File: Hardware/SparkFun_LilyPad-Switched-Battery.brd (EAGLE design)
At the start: 29.4 x 29.2 mm, 11 parts

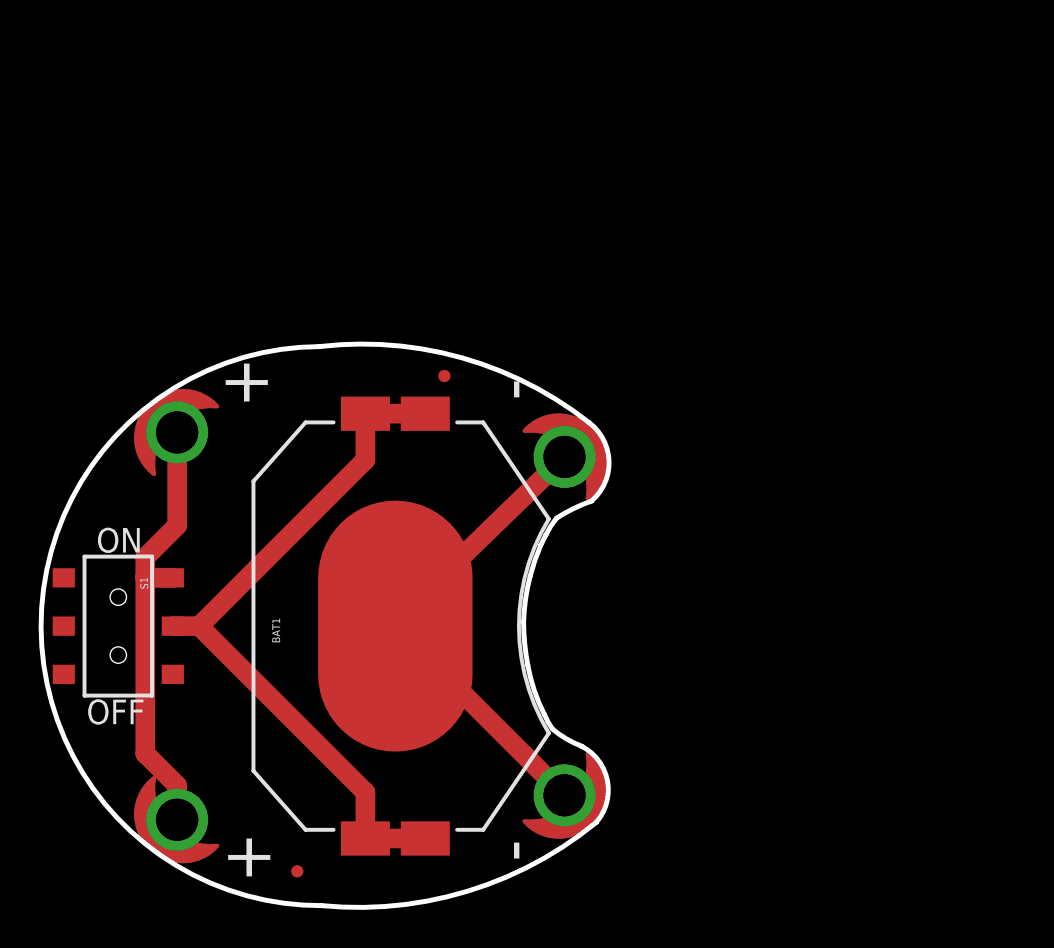
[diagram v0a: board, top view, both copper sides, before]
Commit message: Add board thickness
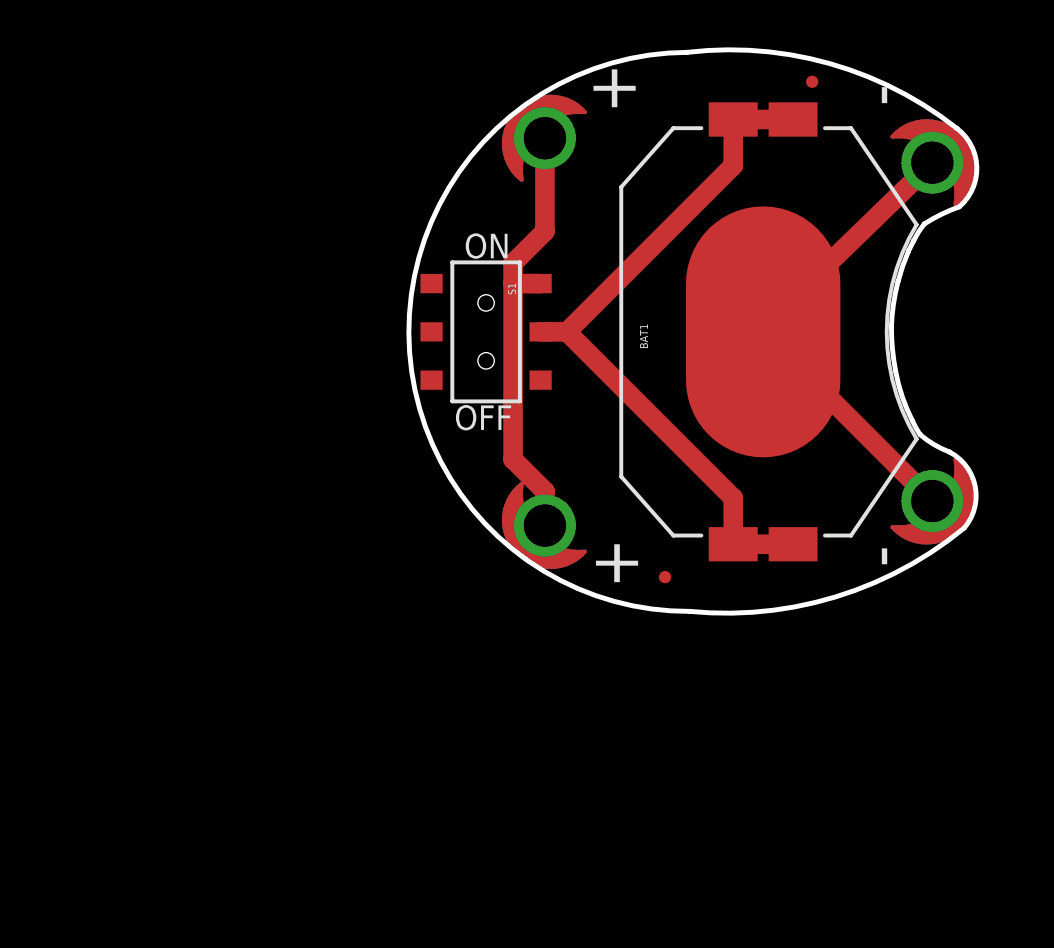
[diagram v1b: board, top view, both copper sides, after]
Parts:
- added LOGO1: SPECIAL_INSTRUCTIONS-ORDERING, SparkFun-Aesthetics:ORDERING_INSTRUCTIONS
- moved U$8 45.8 mm to (44.5, -25.4)
- moved BAT1 24.4 mm to (19.1, 15.2)
- moved JP1 24.4 mm to (14.0, 2.54)
- moved JP2 24.4 mm to (21.6, 28.2)
- moved S1 24.4 mm to (4.70, 15.2)
- moved U$2 24.4 mm to (7.75, 5.21)
- moved U$4 24.4 mm to (7.75, 25.3)
- moved U$5 24.4 mm to (15.2, 15.2)
- moved U$7 24.4 mm to (2.54, 15.2)
- moved U$1 24.4 mm to (27.8, 6.48)
- moved U$3 24.4 mm to (27.8, 24.0)
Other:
- board text added: "Board Thickness is 0.8mm"

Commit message: resolving merge conflicts - again
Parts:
- removed JP1, JP2: FIDUCIALUFIDUCIAL, SparkFun:MICRO-FIDUCIAL
- removed U$2, U$4: SEWTAP6, LilyPad-Wearables:PETAL-SMALL-2SIDE
- removed U$5: LOGO-LPLP, LilyPad-Wearables:LOGO-LILYPAD
- removed U$7: OSHW-LOGOS, SparkFun-Aesthetics:OSHW-LOGO-S
- removed U$8: CREATIVE_COMMONS, SparkFun-Aesthetics:CREATIVE_COMMONS
- added BATB-, BATB-2, BATT+, BATT+2: SEWTAP6, LilyPad-Wearables:PETAL-SMALL-2SIDE
- added FD1, FD2: FIDUCIALUFIDUCIAL, SparkFun-Aesthetics:MICRO-FIDUCIAL
- added FRAME1: FRAME-LETTER, SparkFun-Aesthetics:CREATIVE_COMMONS
- added LOGO2: OSHW-LOGOS, SparkFun-Aesthetics:OSHW-LOGO-S
- BAT1: value (none) -> 20mm coincell
- LOGO1: value SPECIAL_INSTRUCTIONS-ORDERING -> SFE_LOGO_FLAME.1_INCH; device SparkFun-Aesthetics:ORDERING_INSTRUCTIONS -> SparkFun-Aesthetics:SFE_LOGO_FLAME_.1
- S1: device SparkFun:AYZ0202 -> SparkFun-Electromechanical:AYZ0202
- U$1: value SEWTAP6 -> REVISION; device LilyPad-Wearables:PETAL-SMALL-2SIDE -> SparkFun-Aesthetics:REVISION
- U$3: value SEWTAP6 -> (none); device LilyPad-Wearables:PETAL-SMALL-2SIDE -> LilyPad-Wearables:LOGO-LILYPAD
- moved LOGO1 43.7 mm to (11.6, 24.8), flipped to the bottom
- moved U$1 31.4 mm to (2.42, -12.0), turned to 0 degrees
- moved S1 15.6 mm to (16.0, 26.0), turned to 180 degrees
- moved U$3 15.1 mm to (15.8, 14.9), flipped to the bottom, turned to 0 degrees
- moved BAT1 4.98 mm to (16.0, 11.3), turned to 0 degrees
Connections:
- removed net N$3: BAT1.1, BAT1.3, BAT1.P$1, BAT1.P$2, S1.2
- new net GND: BAT1.NEGATIVE, BATB-.1, BATB-2.1
- net N$1: now also BAT1.POSITIVE@1, BAT1.POSITIVE@2, BAT1.POSITIVE@3, BAT1.POSITIVE@4, S1.2; no longer S1.1, U$2.1, U$4.1
- net N$2: now also BATT+.1, BATT+2.1, S1.1; no longer BAT1.2, U$1.1, U$3.1
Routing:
- net N$3: track 36.7 -> 0.00 mm
- net GND: track 0.00 -> 25.2 mm
- net N$1: track 22.9 -> 46.5 mm, vias 0 -> 4
- net N$2: track 26.1 -> 23.4 mm
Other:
- board size 29.4 x 29.2 mm -> 31.8 x 30.1 mm
- board text added: "All Units Inches"
- board text added: "Board Thickness: 0.8mm"
- board text added: "Jim Lindblom"
- board text added: "M. West"
- board text added: "Purple Solder Mask"
- board text added: "ROUTE OUT"
- board text added: "Switched Coin Cell Battery Holder"
- board text added: "v13"
- board text removed: "Board Thickness is 0.8mm"
